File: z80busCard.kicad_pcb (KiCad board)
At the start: 2 copper layers, 115.6 x 78.1 mm, 18 parts, among them J1 Conn_02x20_Odd_Even, J2 Conn_02x20_Odd_Even, J3 Conn_02x20_Odd_Even, J4 Conn_02x20_Odd_Even, J5 USB_C_Receptacle_PowerOnly_6P, SW1 SW_Push

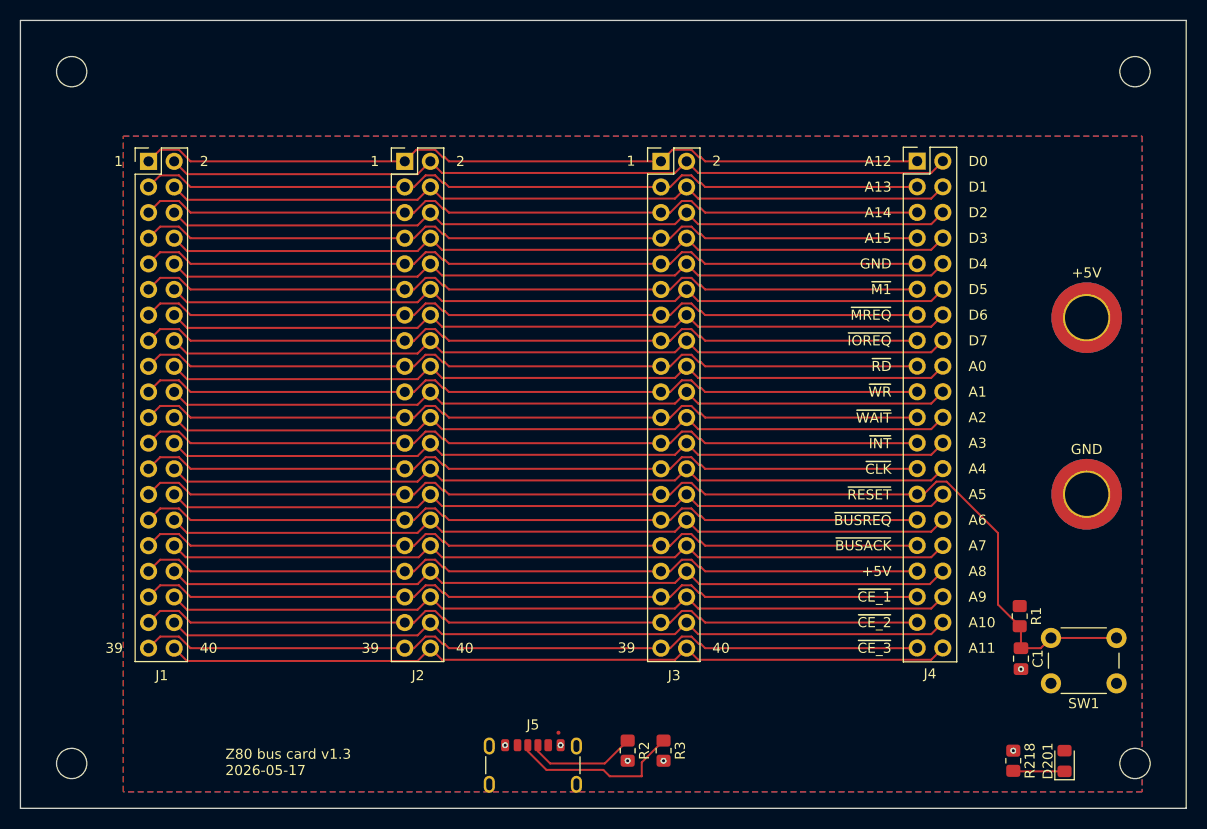
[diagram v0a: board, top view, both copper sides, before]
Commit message: Add RESET inputs and signal conditioning
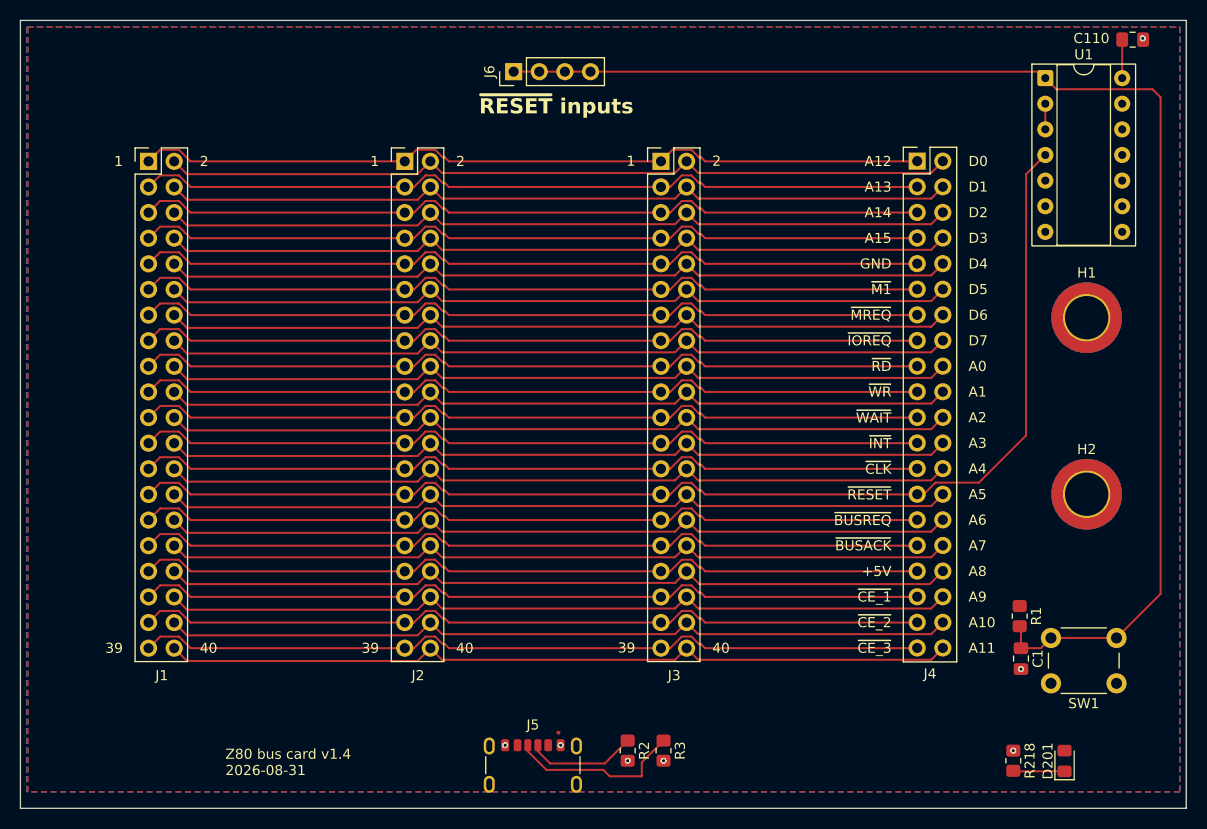
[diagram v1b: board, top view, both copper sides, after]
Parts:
- removed REF** (x4): MountingHole_3mm, MountingHole:MountingHole_3mm
- added C110: 0.1u, Capacitor_SMD:C_0805_2012Metric_Pad1.18x1.45mm_HandSolder, F.Cu at (148.4, 64.1)
- added J6: Conn_01x04_Pin, Connector_PinHeader_2.54mm:PinHeader_1x04_P2.54mm_Vertical, F.Cu at (87.0, 67.3)
- added U1: 74HC14, Package_DIP:DIP-14_W7.62mm_Socket, F.Cu at (139.7, 68.0)
- renumbered +5V to H1, GND to H2
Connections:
- C1 pad 1: /~{RESET} -> /~{RESET_INPUT}
- R1 pad 2: /~{RESET} -> /~{RESET_INPUT}
- SW1 pad 2: /~{RESET} -> /~{RESET_INPUT}
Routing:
- net /~{RESET_INPUT}: track 0.00 -> 132.9 mm
- net /~{RESET}: track 112.2 -> 120.9 mm
- net +5V: track 79.3 -> 83.1 mm
- net Net-(U1-Pad2): track 0.00 -> 2.54 mm
- net GND: track 79.1 -> 79.6 mm, vias 6 -> 7
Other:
- board text added: "Z80 bus card v1.4 2026-08-31"
- board text added: "~{RESET} inputs"
- board text removed: "Z80 bus card v1.3 2026-05-17"

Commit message: Fix vias under pads.  Add mounting holes.
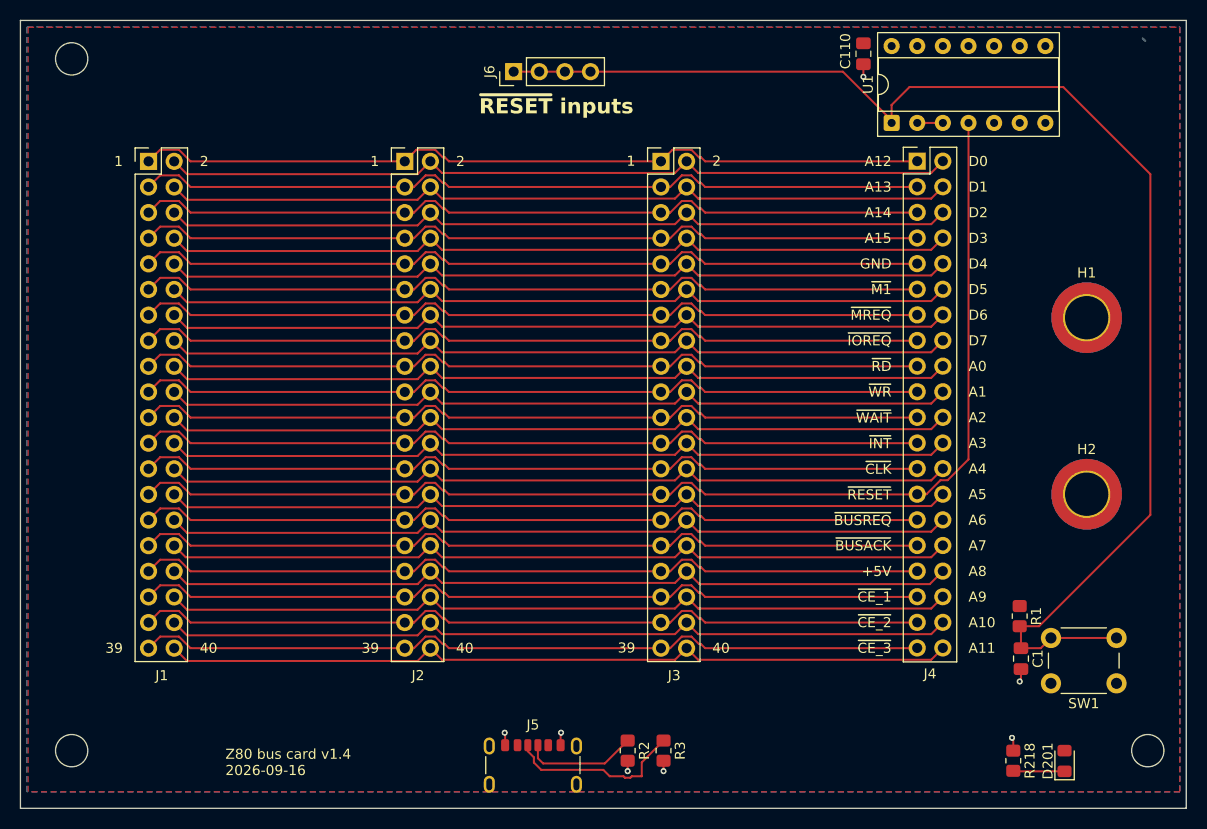
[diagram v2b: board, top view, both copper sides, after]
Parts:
- added REF**: MountingHole_3.2mm_M3, MountingHole:MountingHole_3.2mm_M3, F.Cu at (149.9, 134.6)
- added REF**: MountingHole_3.2mm_M3, MountingHole:MountingHole_3.2mm_M3, F.Cu at (43.2, 134.6)
- added REF**: MountingHole_3.2mm_M3, MountingHole:MountingHole_3.2mm_M3, F.Cu at (43.2, 66.0)
- moved C110 26.7 mm to (121.7, 65.5), turned to -90 degrees
- moved U1 15.9 mm to (124.5, 72.4), turned to 90 degrees
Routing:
- net GND: track 79.6 -> 87.8 mm
- net +5V: track 83.1 -> 79.1 mm
- net /~{RESET}: track 120.9 -> 118.9 mm
- net /~{RESET_INPUT}: track 132.9 -> 134.7 mm
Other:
- board text added: "Z80 bus card v1.4 2026-09-16"
- board text removed: "Z80 bus card v1.4 2026-08-31"

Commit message: Add missing mounting hole
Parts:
- added REF**: MountingHole_3.2mm_M3, MountingHole:MountingHole_3.2mm_M3, F.Cu at (149.9, 66.3)
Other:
- board text added: "Z80 bus card v1.4 WIP yyyy-mm-dd"
- board text removed: "Z80 bus card v1.4 2026-09-16"
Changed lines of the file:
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@@
 		)
 	)
+	(footprint "MountingHole:MountingHole_3.2mm_M3"
+		(layer "F.Cu")
+		(at 149.86 66.294)
+		(descr "Mounting Hole 3.2mm, M3, no annular, generated by kicad-footprint-generator mountinghole.py")
+		(tags "mountinghole M3")
+		(property "Reference" "REF**"
+			(at 0 -4.15 0)
+			(layer "F.SilkS")
+			(hide yes)
+			(effects
+				(font
+					(size 1 1)
+					(thickness 0.15)
+				)
+			)
+		)
+		(property "Value" "MountingHole_3.2mm_M3"
+			(at 0 4.15 0)
+			(layer "F.Fab")
+			(effects
+				(font
+					(size 1 1)
+					(thickness 0.15)
+				)
+			)
+		)
+		(property "Datasheet" ""
+			(at 0 0 0)
+			(layer "F.Fab")
+			(hide yes)
+			(effects
+				(font
+					(size 1.27 1.27)
+				)
+			)
+		)
+		(property "Description" ""
+			(at 0 0 0)
+			(layer "F.Fab")
+			(hide yes)
+			(effects
+				(font
+					(size 1.27 1.27)
+				)
+			)
+		)
+		(property "KiLib_Generator" "mounting_hardware/mounting_hole"
+			(at 0 0 0)
+			(layer "F.SilkS")
+			(hide yes)
+			(effects
+				(font
+					(size 1 1)
+					(thickness 0.15)
+				)
+			)
+		)
+		(attr exclude_from_pos_files exclude_from_bom)
+		(duplicate_pad_numbers_are_jumpers no)
+		(fp_circle
+			(center 0 0)
+			(end 3.2 0)
+			(stroke
+				(width 0.15)
+				(type solid)
+			)
+			(fill no)
+			(layer "Cmts.User")
+		)
+		(fp_circle
+			(center 0 0)
+			(end 3.45 0)
+			(stroke
+				(width 0.05)
+				(type solid)
+			)
+			(fill no)
+			(layer "F.CrtYd")
+		)
+		(fp_text user "${REFERENCE}"
+			(at 0 0 0)
+			(layer "F.Fab")
+			(effects
+				(font
+					(size 1 1)
+					(thickness 0.15)
+				)
+			)
+		)
+		(pad "" np_thru_hole circle
+			(at 0 0)
+			(size 3.2 3.2)
+			(drill 3.2)
+			(layers "*.Cu" "*.Mask")
+		)
+		(embedded_fonts no)
+	)
 	(footprint "Connector_PinHeader_2.54mm:PinHeader_2x20_P2.54mm_Vertical"
 		(layer "F.Cu")
@@
 		)
 		(property "Value" "0.1u"
-			(at 3.5345 -0.127 90)
+			(at -0.508 3.556 90)
 			(layer "F.Fab")
 			(effects
@@
 		)
 	)
-	(gr_text "Z80 bus card v1.4\n2026-09-16"
+	(gr_text "Z80 bus card v1.4 WIP\nyyyy-mm-dd"
 		(at 58.42 137.16 0)
 		(layer "F.SilkS")

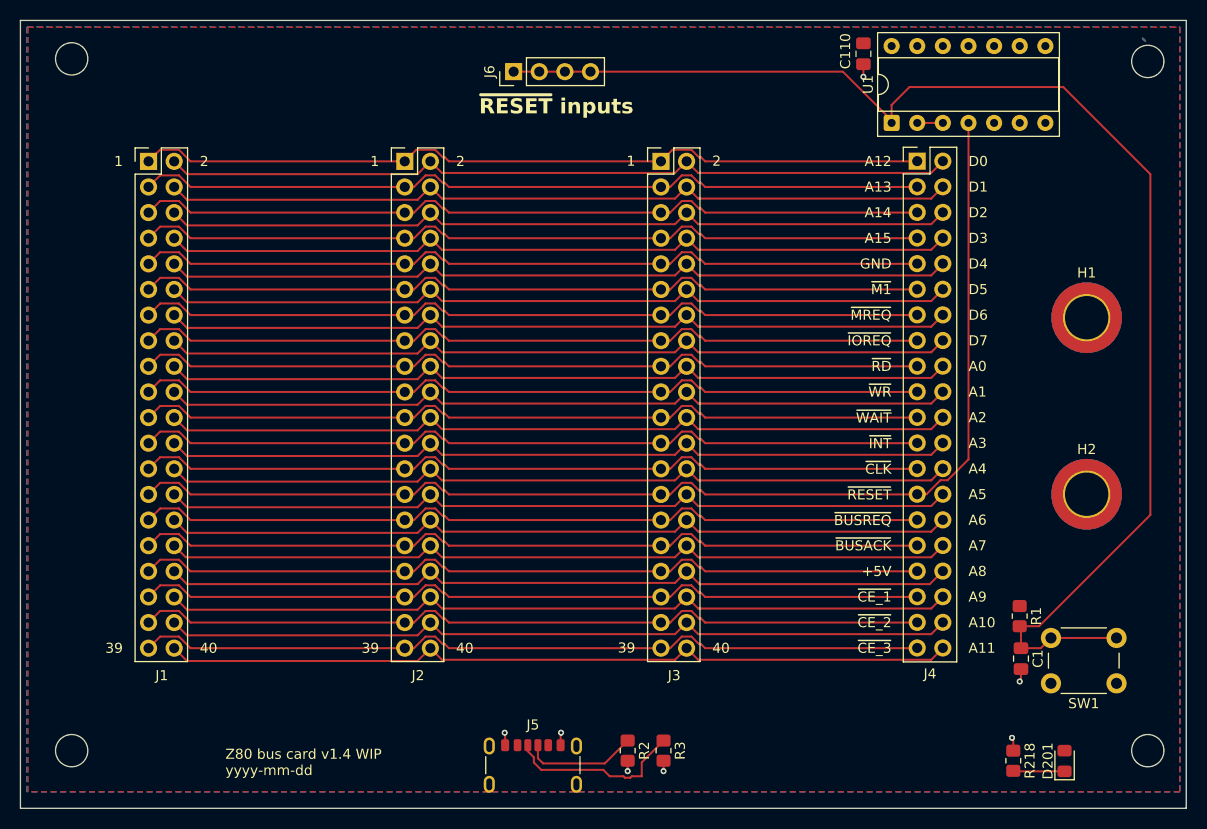
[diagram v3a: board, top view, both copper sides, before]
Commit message: Remove power on reset capacitor
Previously had a 10uF capacitor to GND in parallel with the switch for
automatic power on reset. That effectively smoothed out an incoming low
analog ~{RESET} signal and was therefore removed.
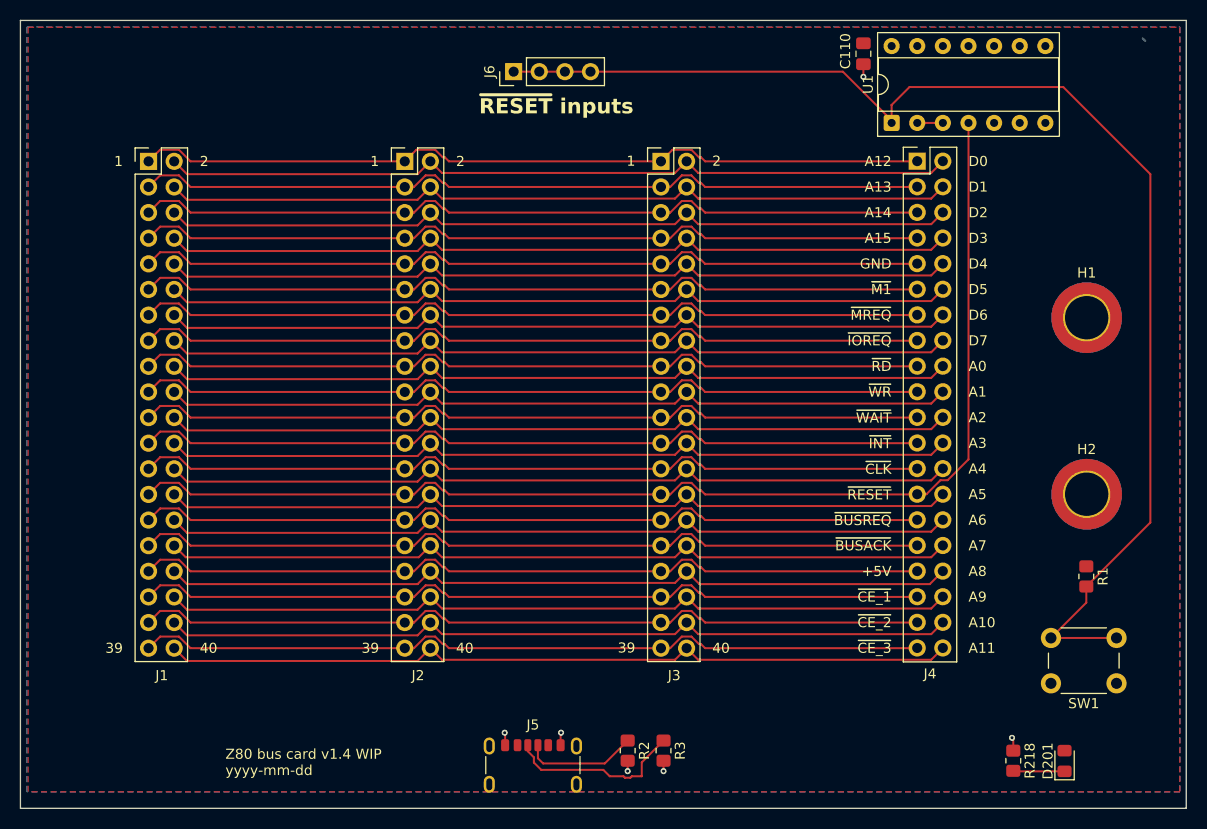
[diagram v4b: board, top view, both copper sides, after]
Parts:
- removed C1: 10u, Capacitor_SMD:C_0805_2012Metric_Pad1.18x1.45mm_HandSolder
- removed REF** (x4): MountingHole_3.2mm_M3, MountingHole:MountingHole_3.2mm_M3
- moved R1 7.69 mm to (143.8, 117.3)
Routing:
- net /~{RESET_INPUT}: track 134.7 -> 128.0 mm
- net GND: track 87.8 -> 86.6 mm, vias 7 -> 6
